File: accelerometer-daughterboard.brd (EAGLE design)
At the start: 17.8 x 25.4 mm, 5 parts, among them U1 LIS3DHTR

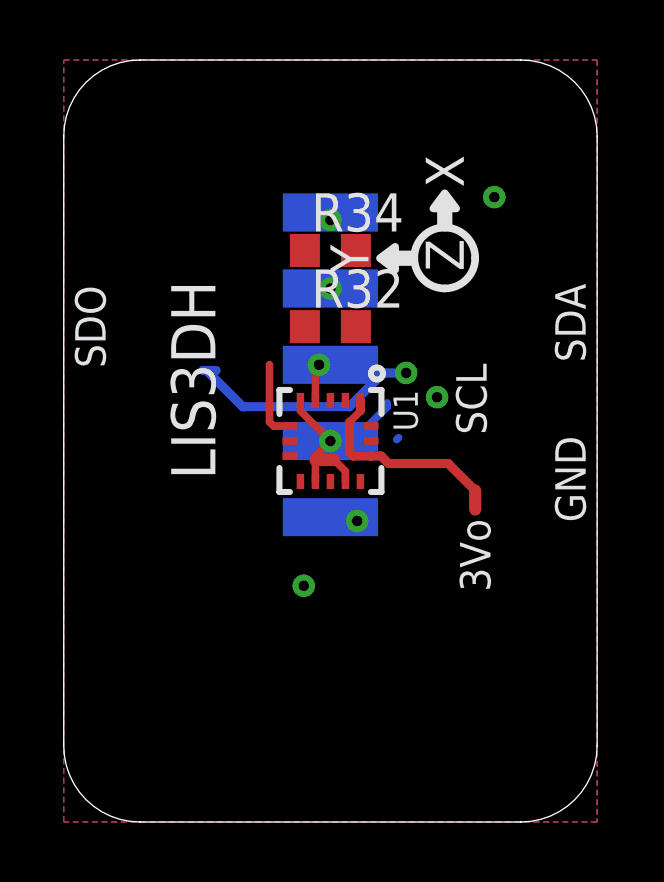
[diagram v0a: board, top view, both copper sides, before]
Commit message: Complete first board draft, including outline and wiring
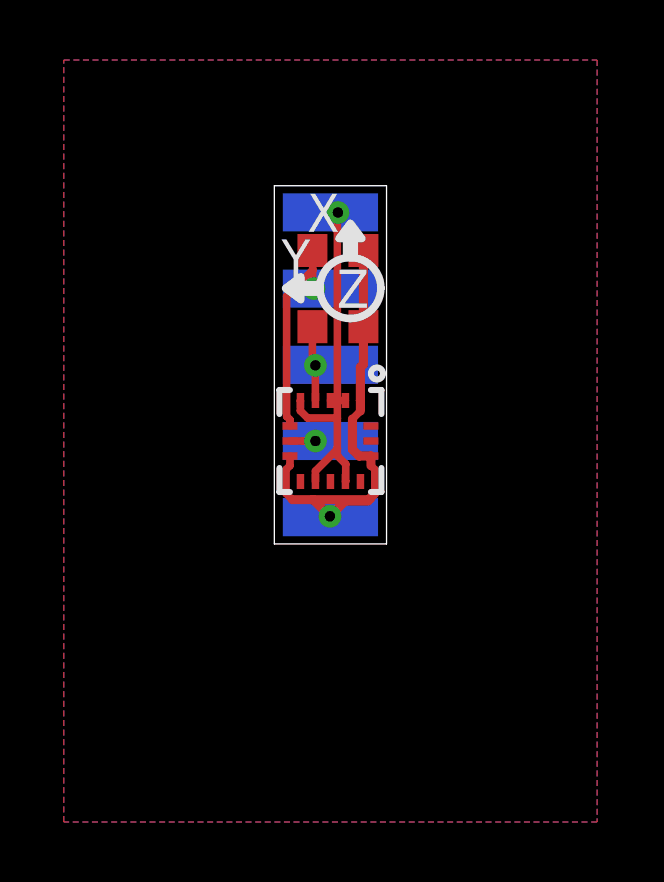
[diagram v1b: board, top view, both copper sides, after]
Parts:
- removed U$25: (no value), microbuilder:PCBFEAT-REV-040
- moved R32 0.25 mm to (9.14, 16.5)
- moved R34 0.25 mm to (9.14, 19.1)
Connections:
- net GND: now also U1.2, U1.3
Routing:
- net GND: track 4.82 -> 12.9 mm, vias 5 -> 1
- net SDA_3V: track 2.65 -> 8.11 mm
- net SDO: track 0.00 -> 1.59 mm
- net SCL_3V: track 1.49 -> 3.01 mm
- net ADC1: track 0.99 -> 0.00 mm
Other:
- board size 17.8 x 25.4 mm -> 3.7 x 11.9 mm
- board text added: "VDD"
- board text removed: "3-axis Accelerometer ±2g/±4g/±8g I2C addr 0x18"
- board text removed: "3Vo"
- board text removed: "GND"
- board text removed: "LIS3DH"
- board text removed: "addr"

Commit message: Rename SD0 to SA0; add measures
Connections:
- net SDO renamed SAO
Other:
- board text added: "SAO"
- board text removed: "SDO"
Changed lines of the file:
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@@
 <wire x1="9.555834375" y1="16.78234375" x2="8.539834375" y2="17.79834375" width="0.254" layer="21" curve="-90"/>
 <wire x1="8.539834375" y1="17.79834375" x2="9.555834375" y2="18.81434375" width="0.254" layer="21" curve="-92"/>
-<text x="8.81850625" y="13.959309375" size="1.016" layer="22" font="vector" ratio="14" rot="MR0" align="center">SDO</text>
+<text x="8.81850625" y="13.959309375" size="1.016" layer="22" font="vector" ratio="14" rot="MR0" align="center">SAO</text>
+<dimension x1="10.760978125" y1="21.208690625" x2="10.75999375" y2="9.27154375" x3="13.9503125" y3="15.239853125" textsize="1.778" layer="21"/>
+<dimension x1="7.021409375" y1="9.268590625" x2="10.7619625" y2="9.26760625" x3="8.890953125" y3="6.496278125" textsize="1.778" layer="21"/>
 </plain>
 <attributes>
@@
 <contactref element="U1" pad="11"/>
 </signal>
-<signal name="SDO">
+<signal name="SAO">
 <contactref element="U1" pad="7"/>
 <contactref element="U$1" pad="P$4"/>
